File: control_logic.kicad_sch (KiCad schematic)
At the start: 6 parts, among them J29 Cmod_A7_Right, J3 Cmod_A7_Left, U3 ESP32-S3-WROOM-1

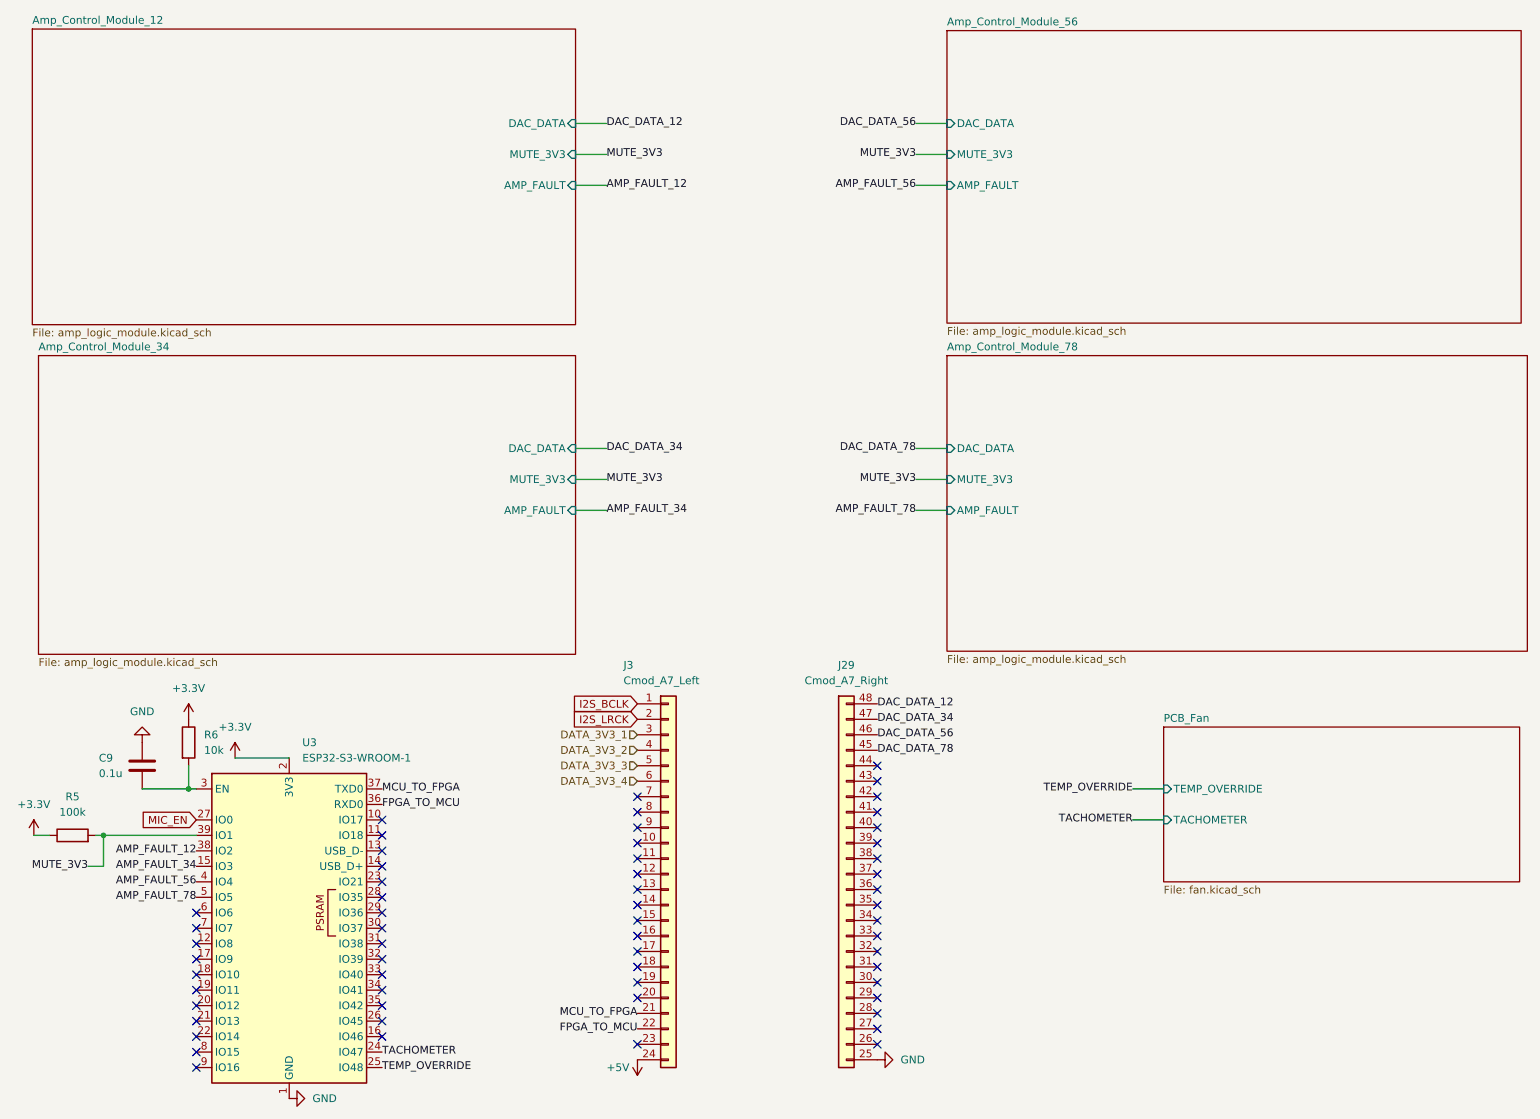
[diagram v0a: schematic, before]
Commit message: Footprinting done (warnings on schematic side but pcb import works fine)
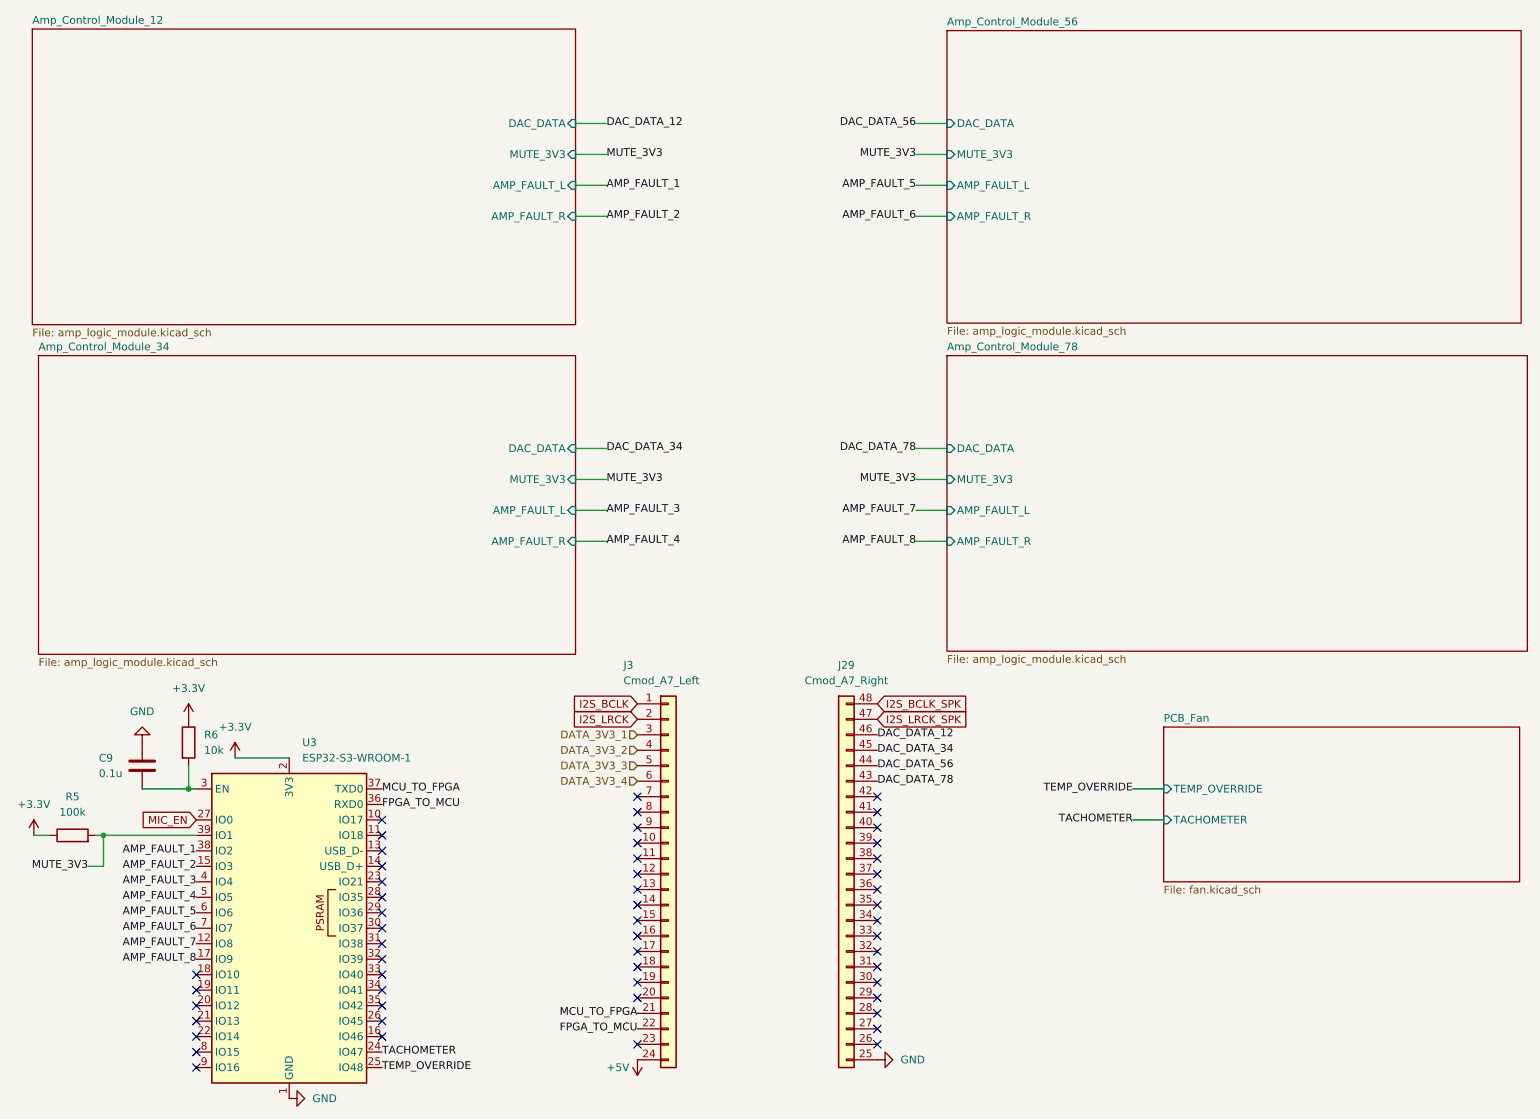
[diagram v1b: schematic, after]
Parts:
- C9: footprint (none) -> Capacitor_SMD:C_0603_1608Metric
- J29: footprint (none) -> Connector:HDR-TH_24P-P2.54-V-F-RIGHT_SIDE_NUMBERING; symbol Cmod_A7_Right:Cmod_A7_Right -> Cmod_A7:Cmod_A7_Right; LCSC Part # (none) -> C41376163
- J3: footprint (none) -> Connector:HDR-TH_24P-P2.54-V-F; symbol Cmod_A7_Right:Cmod_A7_Left -> Cmod_A7:Cmod_A7_Left; LCSC Part # (none) -> C41376163
- R5, R6: footprint (none) -> Resistor_SMD:R_0603_1608Metric
- U3: LCSC Part # (none) -> C2913202
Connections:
- net DAC_DATA_12: now also J29.46 (Pin_22); no longer J29.48 (Pin_24)
- net DAC_DATA_34: now also J29.45 (Pin_21); no longer J29.47 (Pin_23)
- net DAC_DATA_56: now also J29.44 (Pin_20); no longer J29.46 (Pin_22)
- net DAC_DATA_78: now also J29.43 (Pin_19); no longer J29.45 (Pin_21)
- net AMP_FAULT_7: now reaches U3.12 (IO8)
- net AMP_FAULT_8: now reaches U3.17 (IO9)
- net AMP_FAULT_5: now reaches U3.6 (IO6)
- net AMP_FAULT_6: now reaches U3.7 (IO7)
- net AMP_FAULT_12 renamed AMP_FAULT_1
- net AMP_FAULT_34 renamed AMP_FAULT_2
- net AMP_FAULT_56 renamed AMP_FAULT_3
- net AMP_FAULT_78 renamed AMP_FAULT_4
- new net I2S_BCLK_SPK: J29.48 (Pin_24)
- new net I2S_LRCK_SPK: J29.47 (Pin_23)
- no-connect marks 60 -> 54
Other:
- sheet Amp_Control_Module_12 ports: added AMP_FAULT_L, AMP_FAULT_R; removed AMP_FAULT
- sheet Amp_Control_Module_34 ports: added AMP_FAULT_L, AMP_FAULT_R; removed AMP_FAULT
- sheet Amp_Control_Module_56 ports: added AMP_FAULT_L, AMP_FAULT_R; removed AMP_FAULT
- sheet Amp_Control_Module_78 ports: added AMP_FAULT_L, AMP_FAULT_R; removed AMP_FAULT

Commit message: Minor schematic changes
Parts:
- renumbered C9 to C11, J3 to J1, J29 to J2
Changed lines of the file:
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@@
 		(dnp no)
 		(fields_autoplaced yes)
-		(property "Reference" "#PWR024"
+		(property "Reference" "#PWR028"
 			(at 43.18 137.16 0)
 			(effects
@@
 			(project "AEC_Speaker_Mic_System"
 				(path "/b4ee80b5-9d9a-4551-9b0c-6a8cb8d78ca3/b62903f4-3152-49f4-b9de-0aa5889c0444"
-					(reference "#PWR024")
+					(reference "#PWR028")
 					(unit 1)
 				)
@@
 		(on_board yes)
 		(dnp no)
-		(property "Reference" "C9"
+		(property "Reference" "C11"
 			(at 28.448 139.7 0)
 			(effects
@@
 			(project "AEC_Speaker_Mic_System"
 				(path "/b4ee80b5-9d9a-4551-9b0c-6a8cb8d78ca3/b62903f4-3152-49f4-b9de-0aa5889c0444"
-					(reference "C9")
+					(reference "C11")
 					(unit 1)
 				)
@@
 		(on_board yes)
 		(dnp no)
-		(property "Reference" "J3"
+		(property "Reference" "J1"
 			(at 114.554 124.46 0)
 			(effects
@@
 			(project ""
 				(path "/b4ee80b5-9d9a-4551-9b0c-6a8cb8d78ca3/b62903f4-3152-49f4-b9de-0aa5889c0444"
-					(reference "J3")
+					(reference "J1")
 					(unit 1)
 				)
@@
 		(dnp no)
 		(fields_autoplaced yes)
-		(property "Reference" "#PWR026"
+		(property "Reference" "#PWR030"
 			(at 66.04 195.58 0)
 			(effects
@@
 			(project "AEC_Speaker_Mic_System"
 				(path "/b4ee80b5-9d9a-4551-9b0c-6a8cb8d78ca3/b62903f4-3152-49f4-b9de-0aa5889c0444"
-					(reference "#PWR026")
+					(reference "#PWR030")
 					(unit 1)
 				)
@@
 		(dnp no)
 		(fields_autoplaced yes)
-		(property "Reference" "#PWR023"
+		(property "Reference" "#PWR027"
 			(at 35.56 130.81 0)
 			(effects
@@
 			(project "AEC_Speaker_Mic_System"
 				(path "/b4ee80b5-9d9a-4551-9b0c-6a8cb8d78ca3/b62903f4-3152-49f4-b9de-0aa5889c0444"
-					(reference "#PWR023")
+					(reference "#PWR027")
 					(unit 1)
 				)
@@
 		(dnp no)
 		(fields_autoplaced yes)
-		(property "Reference" "#PWR025"
+		(property "Reference" "#PWR029"
 			(at 50.8 143.51 0)
 			(effects
@@
 			(project "AEC_Speaker_Mic_System"
 				(path "/b4ee80b5-9d9a-4551-9b0c-6a8cb8d78ca3/b62903f4-3152-49f4-b9de-0aa5889c0444"
-					(reference "#PWR025")
+					(reference "#PWR029")
 					(unit 1)
 				)
@@
 		(on_board yes)
 		(dnp no)
-		(property "Reference" "#PWR027"
+		(property "Reference" "#PWR031"
 			(at 116.84 185.42 0)
 			(effects
@@
 			(project "AEC_Speaker_Mic_System"
 				(path "/b4ee80b5-9d9a-4551-9b0c-6a8cb8d78ca3/b62903f4-3152-49f4-b9de-0aa5889c0444"
-					(reference "#PWR027")
+					(reference "#PWR031")
 					(unit 1)
 				)
@@
 		(dnp no)
 		(fields_autoplaced yes)
-		(property "Reference" "#PWR022"
+		(property "Reference" "#PWR026"
 			(at 17.78 156.21 0)
 			(effects
@@
 			(project "AEC_Speaker_Mic_System"
 				(path "/b4ee80b5-9d9a-4551-9b0c-6a8cb8d78ca3/b62903f4-3152-49f4-b9de-0aa5889c0444"
-					(reference "#PWR022")
+					(reference "#PWR026")
 					(unit 1)
 				)
@@
 		(on_board yes)
 		(dnp no)
-		(property "Reference" "J29"
+		(property "Reference" "J2"
 			(at 151.13 124.46 0)
 			(effects
@@
 			(project ""
 				(path "/b4ee80b5-9d9a-4551-9b0c-6a8cb8d78ca3/b62903f4-3152-49f4-b9de-0aa5889c0444"
-					(reference "J29")
+					(reference "J2")
 					(unit 1)
 				)
@@
 		(dnp no)
 		(fields_autoplaced yes)
-		(property "Reference" "#PWR028"
+		(property "Reference" "#PWR032"
 			(at 162.56 189.23 0)
 			(effects
@@
 			(project "AEC_Speaker_Mic_System"
 				(path "/b4ee80b5-9d9a-4551-9b0c-6a8cb8d78ca3/b62903f4-3152-49f4-b9de-0aa5889c0444"
-					(reference "#PWR028")
-					(unit 1)
-				)
+					(reference "#PWR032")
+					(unit 1)
+				)
